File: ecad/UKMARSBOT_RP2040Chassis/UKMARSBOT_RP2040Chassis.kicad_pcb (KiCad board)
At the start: 2 copper layers, 99.1 x 81.3 mm, 23 parts, among them J1 CONN_06SILK_FEMALE_PTH, J2 CONN_06SILK_FEMALE_PTH, J3 Conn_01x06, J4 Conn_01x06, J5 Conn_01x03, J6 POWER, J7 Switch, M1 Left MOTOR, M2 Right MOTOR, U1 DVR8833_DC_Controller, U2 LM7805_TO220

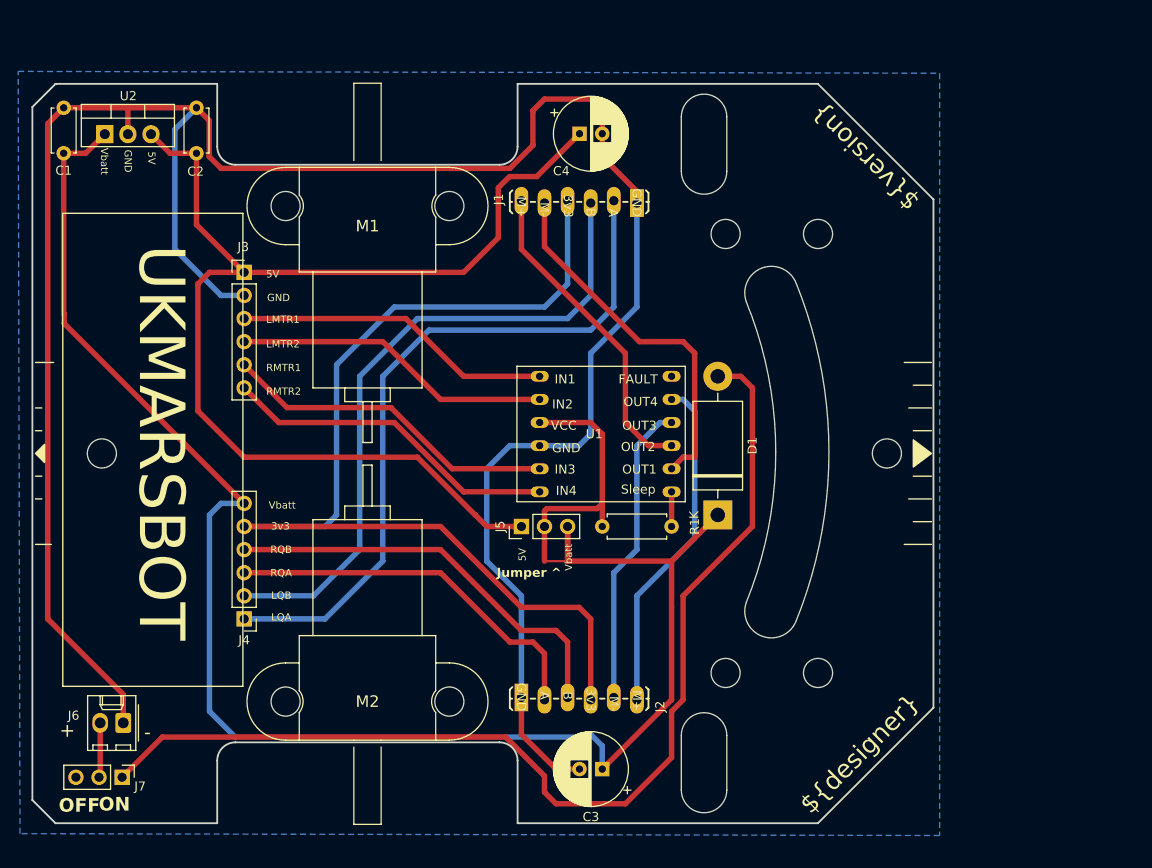
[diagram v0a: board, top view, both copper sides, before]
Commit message: Updated Chassis and Mezzanine board - Sensor boards need to reflect new connector position
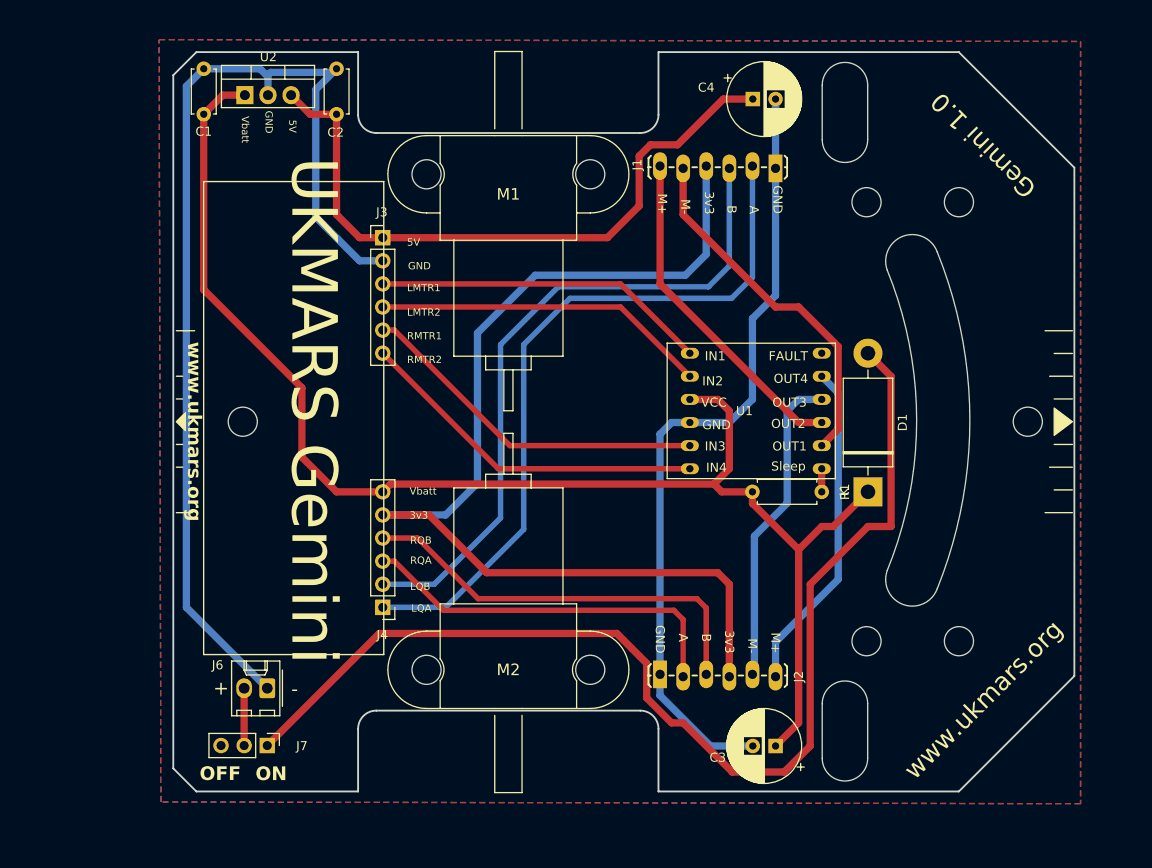
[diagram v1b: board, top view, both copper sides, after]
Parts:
- removed J5: Conn_01x03, Connector_PinHeader_2.54mm:PinHeader_1x03_P2.54mm_Vertical
- moved C4 19.4 mm to (147.4, 66.0)
- moved C3 19.2 mm to (149.9, 137.2)
- moved R1 16.9 mm to (154.9, 109.2)
- moved D1 16.7 mm to (160.0, 109.2)
- moved U1 16.7 mm to (146.4, 100.3)
- moved J7 16.3 mm to (94.0, 137.1)
- moved J6 16.3 mm to (94.0, 130.8)
- moved C1 16.0 mm to (87.0, 67.7)
- moved C2 16.0 mm to (101.6, 67.7)
- moved U2 16.0 mm to (91.5, 65.6)
- moved H3 15.9 mm to (159.9, 77.4)
- moved H4 15.9 mm to (170.0, 77.4)
- moved H1 15.9 mm to (91.3, 101.5)
- moved H2 15.9 mm to (177.6, 101.5)
- moved H5 15.9 mm to (159.9, 125.6)
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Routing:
- net GND: track 262.2 -> 206.1 mm
- net Vbatt: track 210.1 -> 154.3 mm
- net 5V: track 127.9 -> 73.2 mm
- net /PWR: track 117.1 -> 124.4 mm
- net RMTR2: track 37.2 -> 39.0 mm
- net LMTR1: track 35.1 -> 36.9 mm
- net RMTR1: track 37.2 -> 39.0 mm
- net LEFT_MOTOR_2: track 35.3 -> 37.0 mm
- net LMTR2: track 35.1 -> 36.9 mm
- net Vcc: track 116.6 -> 118.2 mm
- net LQB: track 73.1 -> 74.5 mm
- net RIGHT_MOTOR_1: track 33.6 -> 34.9 mm
- net Net-(U1-SLEEP): track 3.81 -> 2.54 mm
- net LQA: track 78.4 -> 79.6 mm
- net LEFT_MOTOR_1: track 40.7 -> 39.8 mm
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- added copper zone on F.Cu, net GND
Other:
- board text added: "Gemini 1.0"
- board text added: "UKMARS Gemini"
- board text added: "www.ukmars.org"
- board text removed: "${designer}"
- board text removed: "${version}"
- board text removed: "Jumper ^"
- board text removed: "Jumper^"
- board text removed: "PTO"
- board text removed: "UKMARSBOT"
- board text removed: "UKMARSBOT v2"
- board text removed: "ukmars.org"

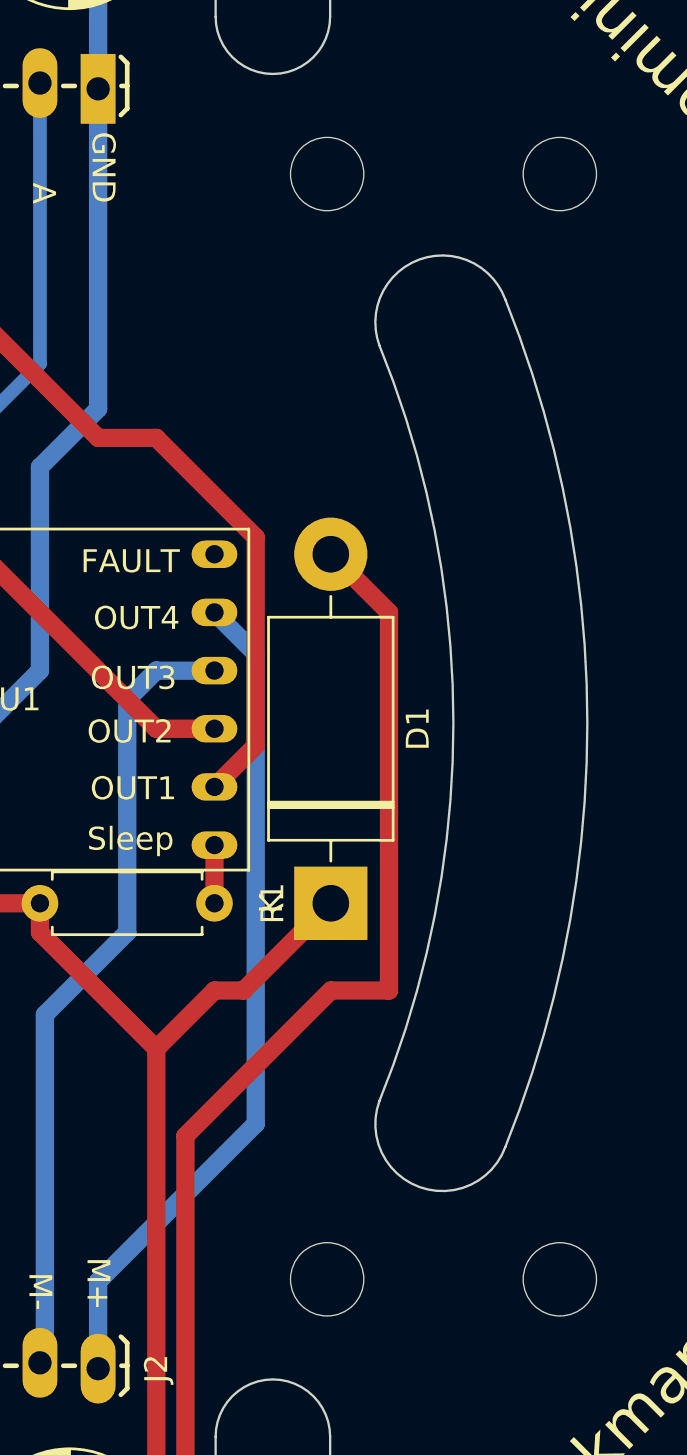
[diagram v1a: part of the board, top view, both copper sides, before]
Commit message: Revised lime sensor board and sensor mounting hole moved forward 1.27mm for connector
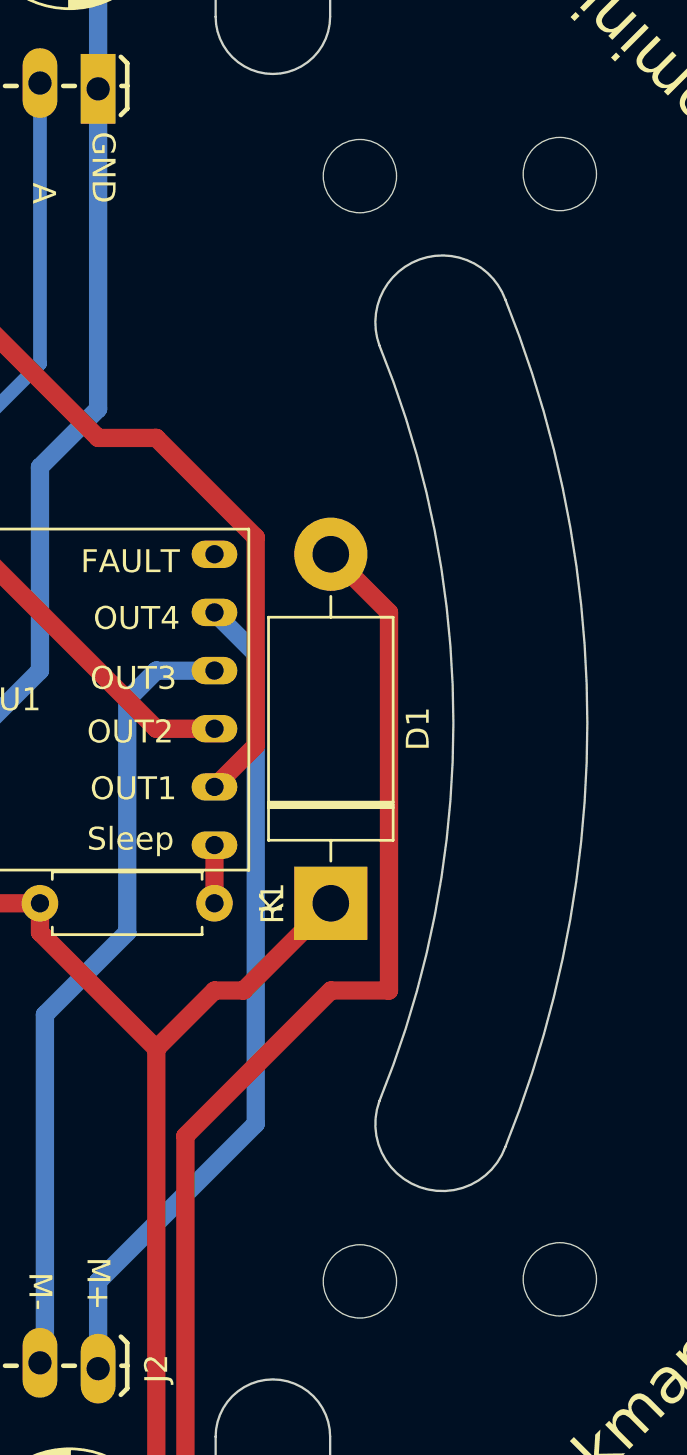
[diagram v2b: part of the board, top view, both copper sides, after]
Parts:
- moved H3 1.43 mm to (161.3, 77.5)
- moved H5 1.43 mm to (161.3, 125.7)
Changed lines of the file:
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@@
 	(footprint "ukmarsbot:MountingHole_3.2mm_M3_clearance"
 		(layer "F.Cu")
-		(at 159.86 125.64)
+		(at 161.29 125.73)
 		(descr "Mounting Hole 3.2mm, no annular, M3")
 		(tags "mounting hole 3.2mm no annular m3")
@@
 	(footprint "ukmarsbot:MountingHole_3.2mm_M3_clearance"
 		(layer "F.Cu")
-		(at 159.86 77.38)
+		(at 161.29 77.47)
 		(descr "Mounting Hole 3.2mm, no annular, M3")
 		(tags "mounting hole 3.2mm no annular m3")

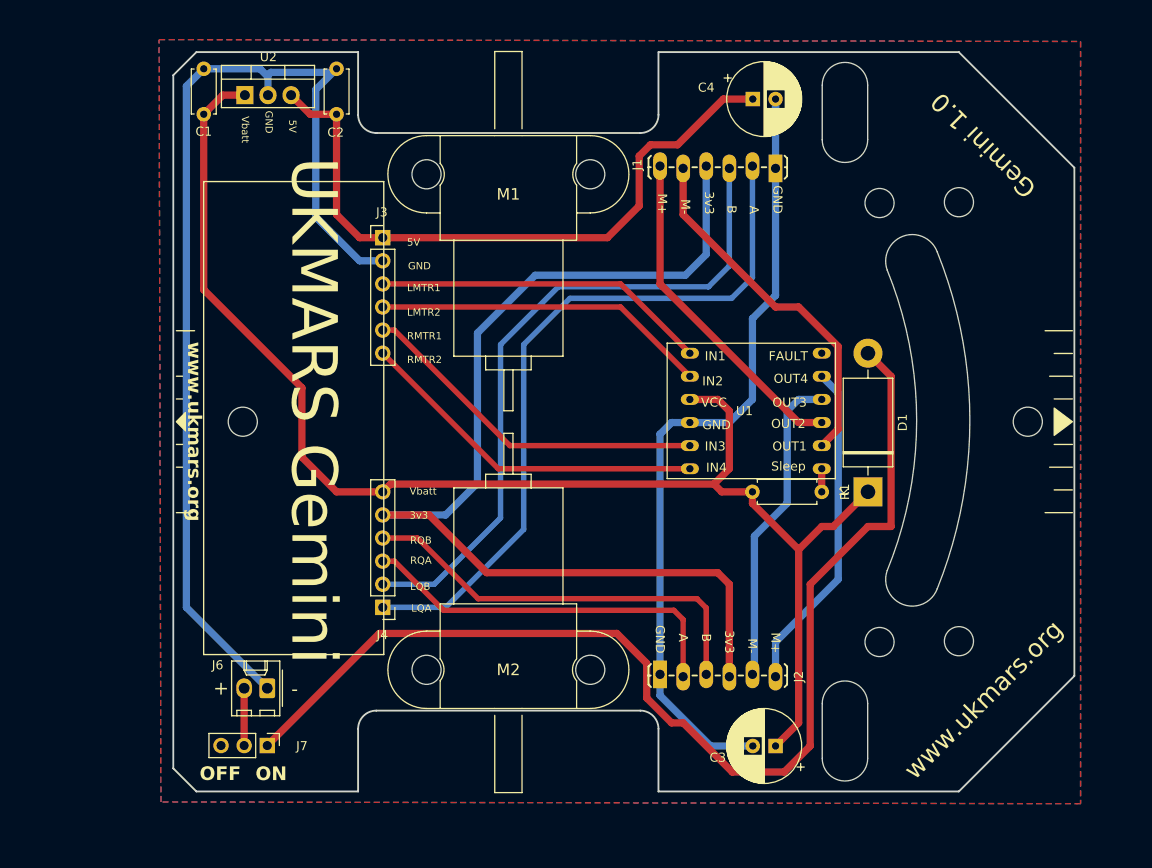
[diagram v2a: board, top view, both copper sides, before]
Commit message: Revised Wall Sensor Board consistent with hole and connector position. Fabrication files created.
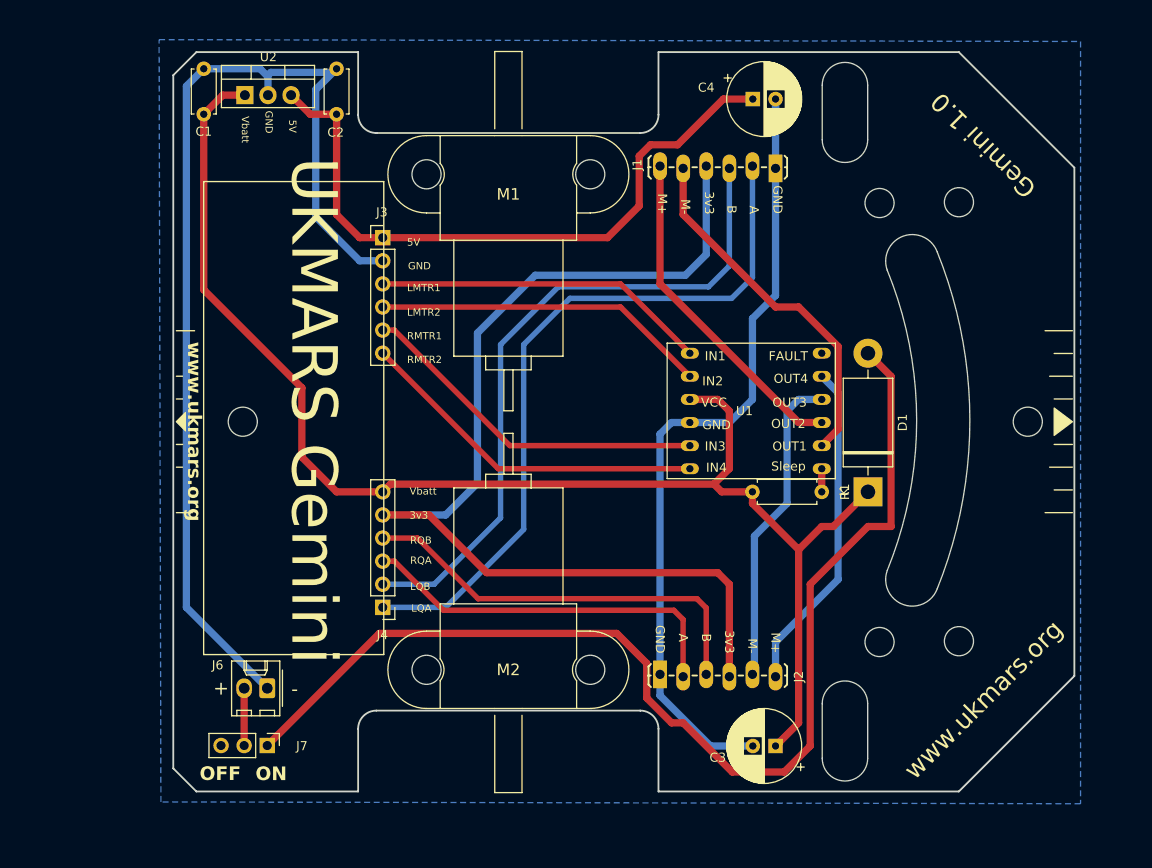
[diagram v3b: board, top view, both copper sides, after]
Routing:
- removed copper zone on F.Cu, net GND
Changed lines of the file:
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@@
 			(outputformat 1)
 			(mirror no)
-			(drillshape 1)
+			(drillshape 0)
 			(scaleselection 1)
-			(outputdirectory "")
+			(outputdirectory "fab/")
 		)
 	)
@@
 		(net 1)
 		(net_name "GND")
-		(layers "F&B.Cu")
+		(layer "B.Cu")
 		(hatch edge 0.508)
 		(connect_pads

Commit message: Reworked chassis board for production
Board reworked based on known issues from prototype builds.
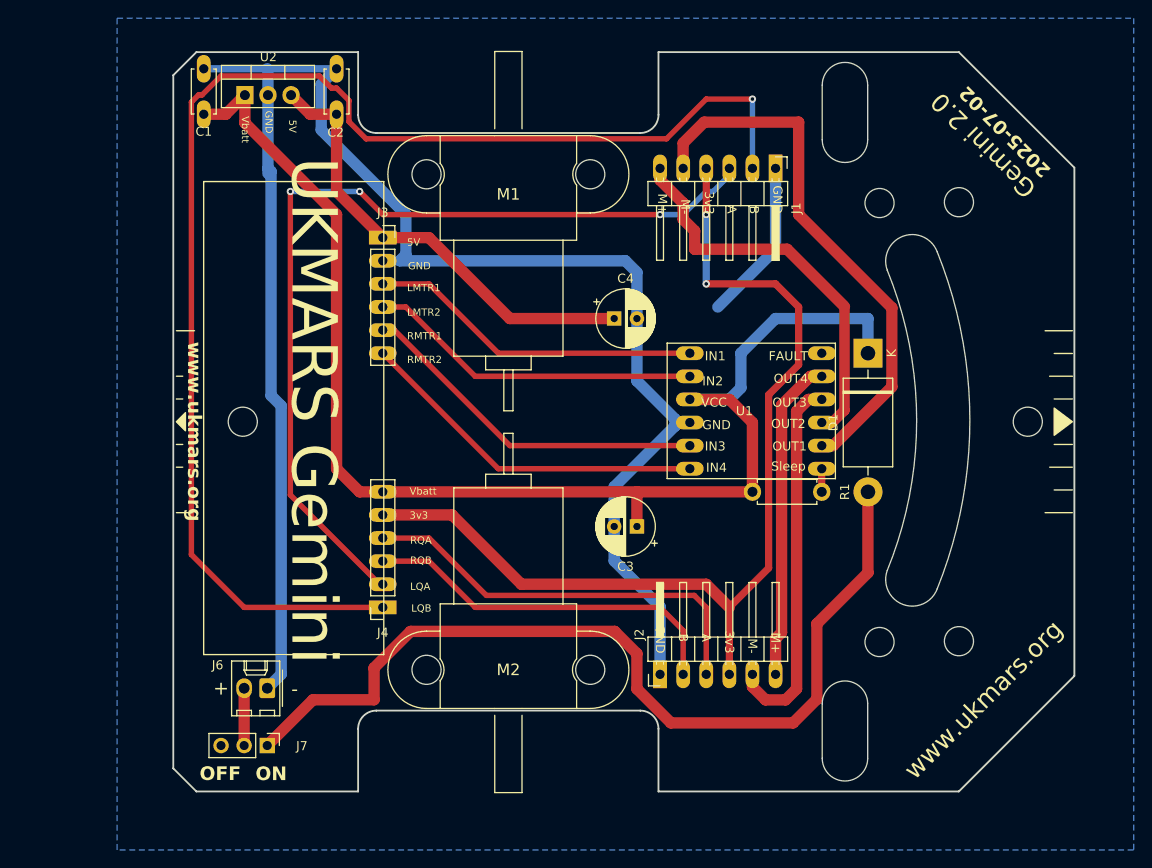
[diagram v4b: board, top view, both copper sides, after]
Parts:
- C3: value 330uF, 16V -> 100uF,16V; footprint Capacitor_THT:CP_Radial_D8.0mm_P2.50mm -> Capacitor_THT:CP_Radial_D6.3mm_P2.50mm
- C4: value 330uF, 16V -> 100uF, 16V; footprint Capacitor_THT:CP_Radial_D8.0mm_P2.50mm -> Capacitor_THT:CP_Radial_D6.3mm_P2.50mm
- J1, J2: footprint ukmarsbot:1X06_LOCK_LONGPADS -> Connector_PinHeader_2.54mm:PinHeader_1x06_P2.54mm_Horizontal
- J3, J4: footprint Connector_PinHeader_2.54mm:PinHeader_1x06_P2.54mm_Vertical -> Connector_PinSocket_2.54mm:PinSocket_1x06_P2.54mm_Vertical
- moved C3 28.5 mm to (134.6, 113.0)
- moved C4 28.5 mm to (132.1, 90.2)
- moved D1 15.2 mm to (160.0, 94.0), turned to -90 degrees
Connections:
- J1 pad 2: LQA -> LQB
- J1 pad 3: LQB -> LQA
- J2 pad 2: RQA -> RQB
- J2 pad 3: RQB -> RQA
- J4 pad 1: LQA -> LQB
- J4 pad 2: LQB -> LQA
- J4 pad 3: RQA -> RQB
- J4 pad 4: RQB -> RQA
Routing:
- net LQB: track 74.5 -> 149.5 mm, vias 0 -> 1
- net /PWR: track 124.4 -> 100.8 mm
- net 5V: track 73.2 -> 50.7 mm
- net LQA: track 79.6 -> 100.5 mm, vias 0 -> 3
- net LEFT_MOTOR_1: track 39.8 -> 60.2 mm
- net Vbatt: track 154.3 -> 146.1 mm
- net RIGHT_MOTOR_1: track 34.9 -> 43.0 mm
- net Vcc: track 118.2 -> 110.3 mm, vias 0 -> 2
- net LEFT_MOTOR_2: track 37.0 -> 44.3 mm
- net RQB: track 46.0 -> 41.3 mm
- net RQA: track 42.0 -> 45.8 mm
- net GND: track 206.1 -> 209.2 mm
- net RIGHT_MOTOR_2: track 36.6 -> 35.9 mm
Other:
- board text added: "2025-07-02"
- board text added: "Gemini 2.0"
- board text removed: "Gemini 1.0"

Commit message: Add v2 wall sensor board
Wall sensor updated for Issues raised on prototype builds. Better pin markings added to Line sensor, mezz and chassis boards
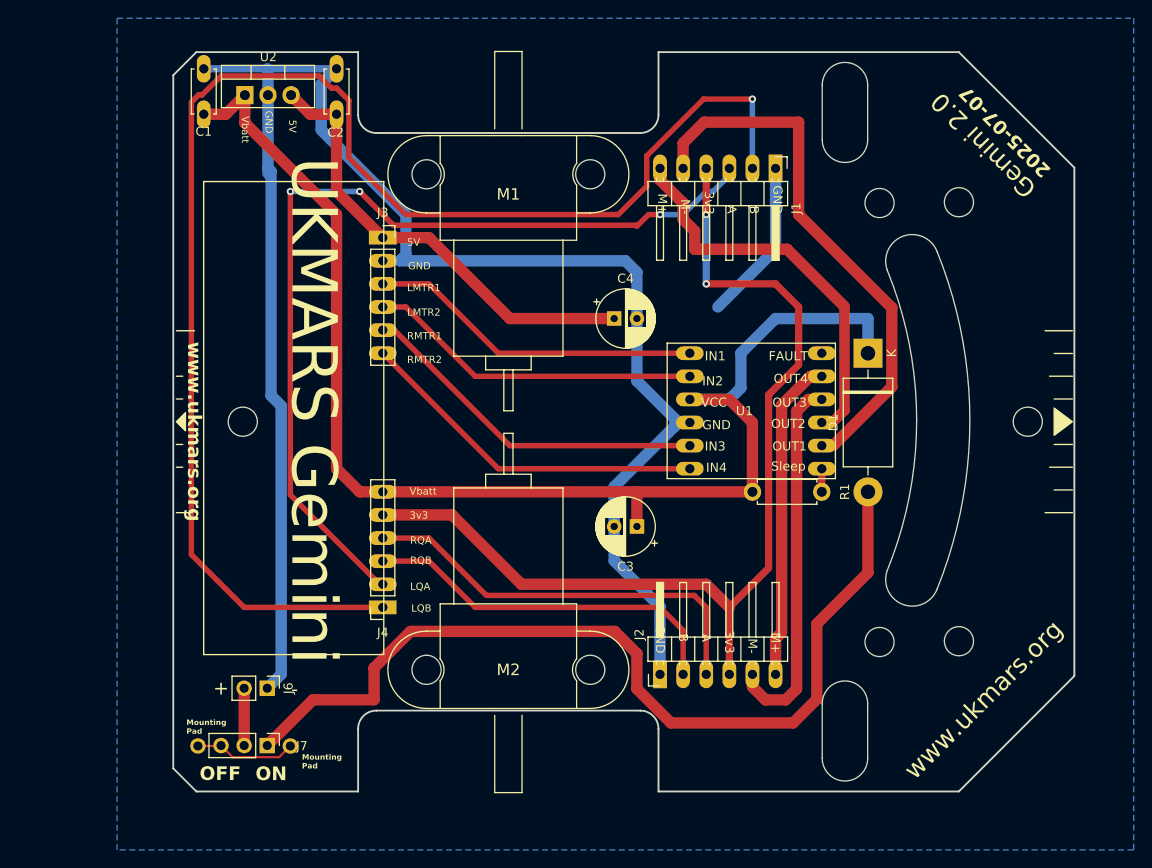
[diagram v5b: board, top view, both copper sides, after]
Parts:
- added ?: , , F.Cu at (86.4, 137.2)
- added ?: , , F.Cu at (96.5, 137.2)
- J6: footprint Connector_Molex:Molex_KK-254_AE-6410-02A_1x02_P2.54mm_Vertical -> Connector_PinHeader_2.54mm:PinHeader_1x02_P2.54mm_Vertical
- turned J6 to -90 degrees
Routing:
- net unconnected-(J7-Pin_3-Pad3): track 0.00 -> 11.2 mm
- net LQB: track 149.5 -> 160.6 mm
- net LQA: track 100.5 -> 101.5 mm
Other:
- board text added: "2025-07-07"
- board text added: "Mounting Pad"
- board text removed: "2025-07-02"
